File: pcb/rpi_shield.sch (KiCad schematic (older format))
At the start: 7 parts, among them P101 CONN_01X08, P102 CONN_02X20

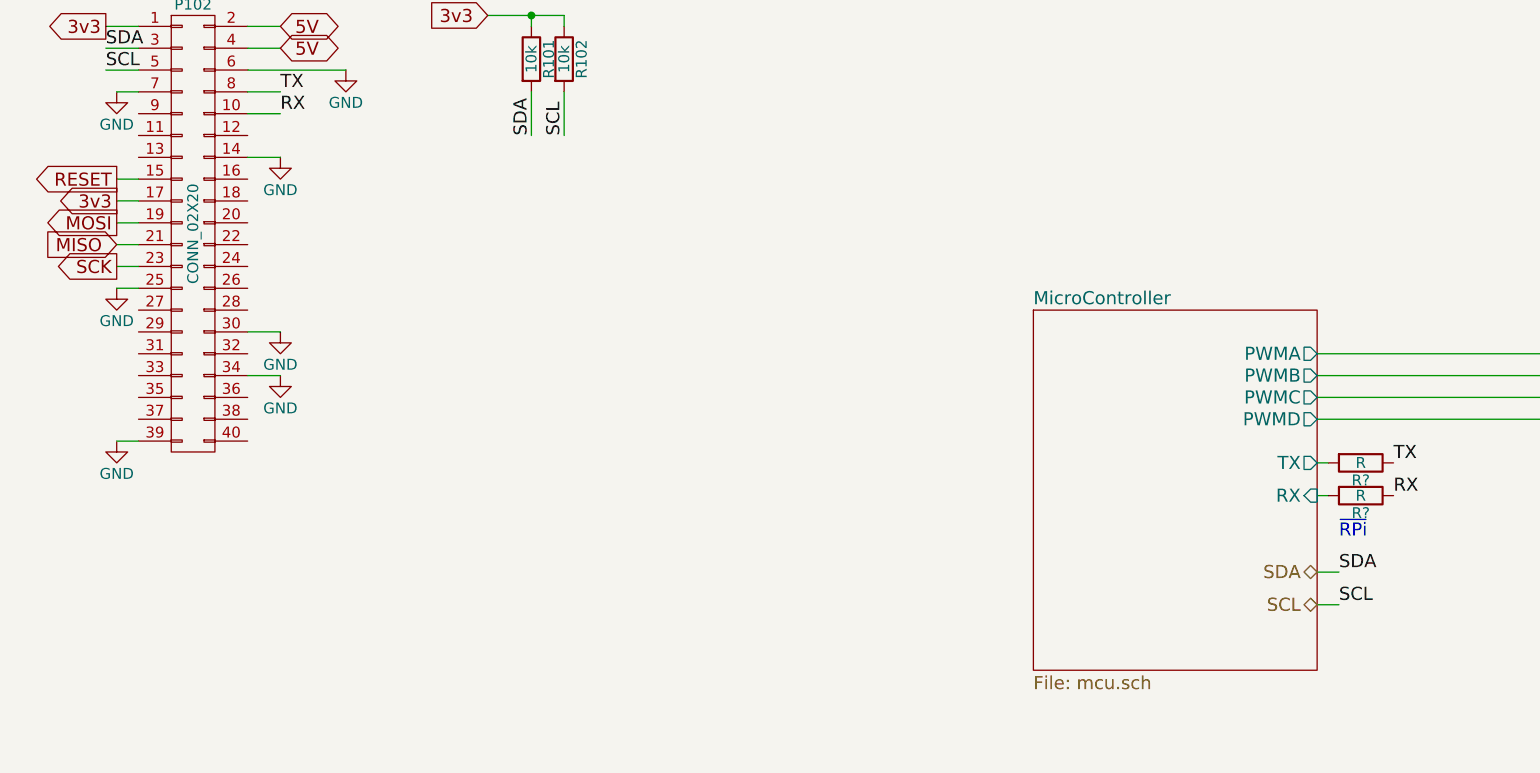
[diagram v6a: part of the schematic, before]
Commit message: removed resistor dividors, added cap to usb
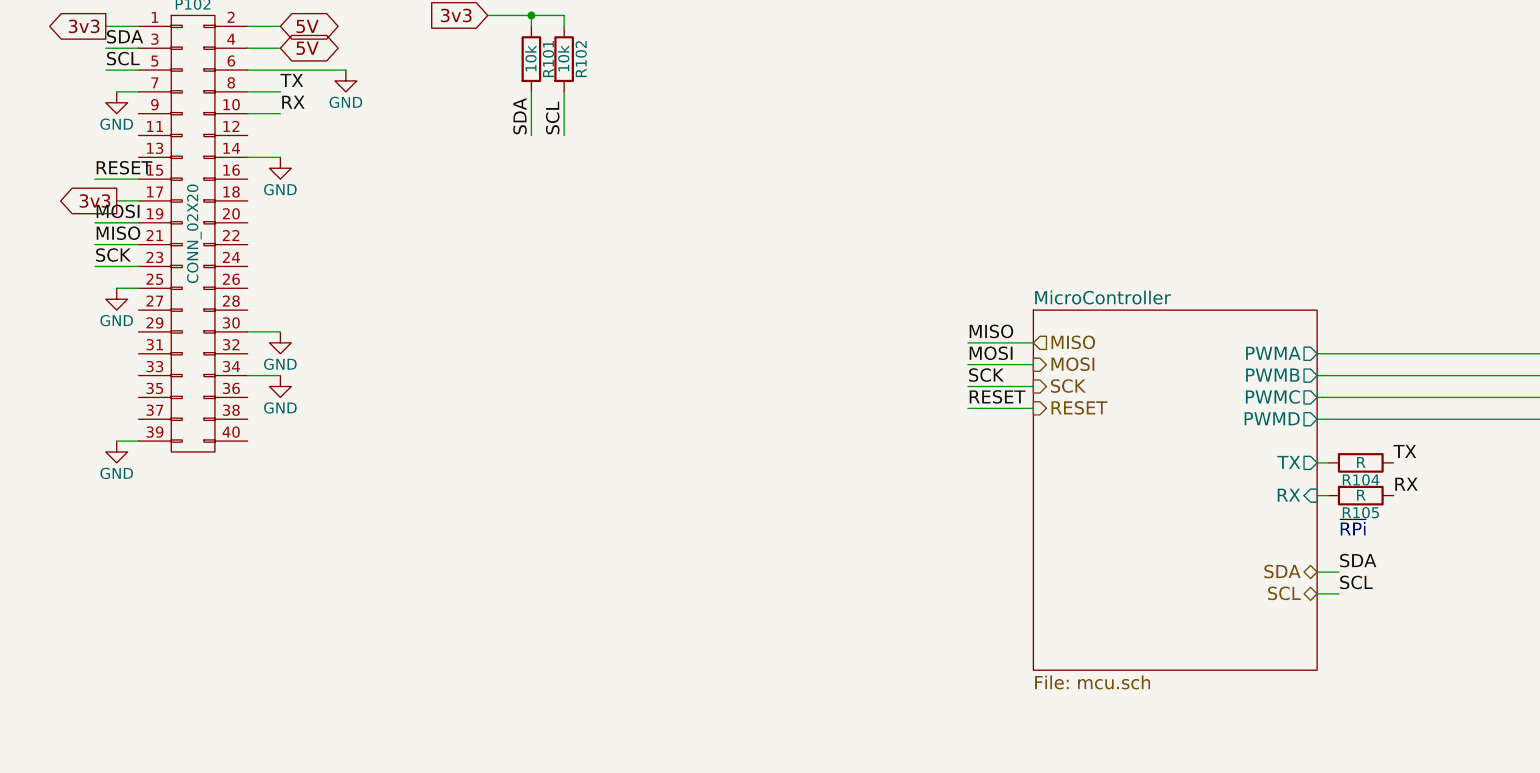
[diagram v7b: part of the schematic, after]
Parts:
- R104, R105: renamed from R?; footprint (none) -> netl:SMD_0603
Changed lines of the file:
@@
 	1500 1200 1350 1200
 $Comp
-L GND #PWR107
+L GND #PWR01
 U 1 1 566A0FDB
 P 2450 1400
-F 0 "#PWR107" H 2450 1150 50  0001 C CNN
+F 0 "#PWR01" H 2450 1150 50  0001 C CNN
 F 1 "GND" H 2450 1250 50  0000 C CNN
 F 2 "" H 2450 1400 60  0000 C CNN
@@
 $EndComp
 $Comp
-L GND #PWR101
+L GND #PWR02
 U 1 1 566A102A
 P 1400 1500
-F 0 "#PWR101" H 1400 1250 50  0001 C CNN
+F 0 "#PWR02" H 1400 1250 50  0001 C CNN
 F 1 "GND" H 1400 1350 50  0000 C CNN
 F 2 "" H 1400 1500 60  0000 C CNN
@@
 	2450 1400 2000 1400
 $Comp
-L GND #PWR104
+L GND #PWR03
 U 1 1 566A10C5
 P 2150 1800
-F 0 "#PWR104" H 2150 1550 50  0001 C CNN
+F 0 "#PWR03" H 2150 1550 50  0001 C CNN
 F 1 "GND" H 2150 1650 50  0000 C CNN
 F 2 "" H 2150 1800 60  0000 C CNN
@@
 	2150 1800 2000 1800
 $Comp
-L GND #PWR105
+L GND #PWR04
 U 1 1 566A110F
 P 2150 2600
-F 0 "#PWR105" H 2150 2350 50  0001 C CNN
+F 0 "#PWR04" H 2150 2350 50  0001 C CNN
 F 1 "GND" H 2150 2450 50  0000 C CNN
 F 2 "" H 2150 2600 60  0000 C CNN
@@
 	2150 2600 2000 2600
 $Comp
-L GND #PWR106
+L GND #PWR05
 U 1 1 566A116A
 P 2150 2800
-F 0 "#PWR106" H 2150 2550 50  0001 C CNN
+F 0 "#PWR05" H 2150 2550 50  0001 C CNN
 F 1 "GND" H 2150 2650 50  0000 C CNN
 F 2 "" H 2150 2800 60  0000 C CNN
@@
 	2150 2800 2000 2800
 $Comp
-L GND #PWR103
+L GND #PWR06
 U 1 1 566A11B6
 P 1400 3100
-F 0 "#PWR103" H 1400 2850 50  0001 C CNN
+F 0 "#PWR06" H 1400 2850 50  0001 C CNN
 F 1 "GND" H 1400 2950 50  0000 C CNN
 F 2 "" H 1400 3100 60  0000 C CNN
@@
 	1500 3100 1400 3100
 $Comp
-L GND #PWR102
+L GND #PWR07
 U 1 1 566A1203
 P 1400 2400
-F 0 "#PWR102" H 1400 2150 50  0001 C CNN
+F 0 "#PWR07" H 1400 2150 50  0001 C CNN
 F 1 "GND" H 1400 2250 50  0000 C CNN
 F 2 "" H 1400 2400 60  0000 C CNN
@@
 Wire Wire Line
 	1500 2000 1400 2000
-Text GLabel 1400 2300 0    60   Output ~ 0
-SCK
-Text GLabel 1400 2100 0    60   Output ~ 0
-MOSI
-Text GLabel 1400 2200 0    60   Input ~ 0
-MISO
-Wire Wire Line
-	1500 2300 1400 2300
-Wire Wire Line
-	1400 2200 1500 2200
-Wire Wire Line
-	1500 2100 1400 2100
-Text GLabel 1400 1900 0    60   Output ~ 0
-RESET
-Wire Wire Line
-	1500 1900 1400 1900
+Wire Wire Line
+	1500 2300 1300 2300
+Wire Wire Line
+	1300 2200 1500 2200
+Wire Wire Line
+	1500 2100 1300 2100
+Wire Wire Line
+	1500 1900 1300 1900
 $Sheet
 S 9150 1350 1100 1850
@@
 $EndComp
 $Comp
-L GND #PWR108
+L GND #PWR08
 U 1 1 56C24834
 P 8050 1250
-F 0 "#PWR108" H 8050 1000 50  0001 C CNN
+F 0 "#PWR08" H 8050 1000 50  0001 C CNN
 F 1 "GND" H 8050 1100 50  0000 C CNN
 F 2 "" H 8050 1250 60  0000 C CNN
@@
 	9150 3000 6900 3000
 $Comp
-L R R?
+L R R104
 U 1 1 570D5FBE
 P 7100 3200
-F 0 "R?" V 7180 3200 50  0000 C CNN
+F 0 "R104" V 7180 3200 50  0000 C CNN
 F 1 "R" V 7100 3200 50  0000 C CNN
-F 2 "" V 7030 3200 50  0000 C CNN
+F 2 "netl:SMD_0603" V 7030 3200 50  0001 C CNN
 F 3 "" H 7100 3200 50  0000 C CNN
 	1    7100 3200
@@
 $EndComp
 $Comp
-L R R?
+L R R105
 U 1 1 570D60AE
 P 7100 3350
-F 0 "R?" V 7180 3350 50  0000 C CNN
+F 0 "R105" V 7180 3350 50  0000 C CNN
 F 1 "R" V 7100 3350 50  0000 C CNN
-F 2 "" V 7030 3350 50  0000 C CNN
+F 2 "netl:SMD_0603" V 7030 3350 50  0001 C CNN
 F 3 "" H 7100 3350 50  0000 C CNN
 	1    7100 3350
@@
 Text HLabel 6900 3700 0    60   BiDi ~ 0
 SDA
-Text HLabel 6900 3850 0    60   BiDi ~ 0
+Text HLabel 6900 3800 0    60   BiDi ~ 0
 SCL
 Text Label 7000 3700 0    60   ~ 0
@@
 	6900 3700 7000 3700
 Wire Wire Line
-	6900 3850 7000 3850
-Text Label 7000 3850 0    60   ~ 0
+	6900 3800 7000 3800
+Text Label 7000 3800 0    60   ~ 0
 SCL
 Text Label 3300 1700 1    60   ~ 0
@@
 Wire Wire Line
 	9150 2450 8950 2450
+Text HLabel 5600 2650 2    60   Input ~ 0
+MISO
+Text HLabel 5600 2750 2    60   Output ~ 0
+MOSI
+Text HLabel 5600 2850 2    60   Output ~ 0
+SCK
+Text HLabel 5600 2950 2    60   Output ~ 0
+RESET
+Text Label 1300 2100 0    60   ~ 0
+MOSI
+Text Label 1300 2200 0    60   ~ 0
+MISO
+Text Label 1300 2300 0    60   ~ 0
+SCK
+Text Label 1300 1900 0    60   ~ 0
+RESET
+Wire Wire Line
+	5600 2650 5300 2650
+Wire Wire Line
+	5600 2750 5300 2750
+Wire Wire Line
+	5600 2850 5300 2850
+Wire Wire Line
+	5600 2950 5300 2950
+Text Label 5300 2950 0    60   ~ 0
+RESET
+Text Label 5300 2750 0    60   ~ 0
+MOSI
+Text Label 5300 2650 0    60   ~ 0
+MISO
+Text Label 5300 2850 0    60   ~ 0
+SCK
 $EndSCHEMATC

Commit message: added mcu
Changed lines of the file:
@@
 VCC
 Wire Wire Line
-	8250 1150 8250 1250
-Wire Wire Line
-	8250 1250 8250 1300
+	8250 1150 8250 1300
 Wire Wire Line
 	8150 1150 8150 1250
@@
 3v3
 Wire Wire Line
-	3100 1150 3300 1150
-Wire Wire Line
-	3300 1150 3450 1150
+	3100 1150 3450 1150
 Wire Wire Line
 	3450 1150 3450 1200
@@
 	3300 1200 3300 1150
 Connection ~ 3300 1150
-$Sheet
-S 5600 2500 1300 1650
-U 570D51C9
-F0 "MicroController" 60
-F1 "mcu.sch" 60
-F2 "PWMA" O R 6900 2700 60
-F3 "PWMB" O R 6900 2800 60
-F4 "PWMC" O R 6900 2900 60
-F5 "PWMD" O R 6900 3000 60
-F6 "TX" O R 6900 3200 60
-F7 "RX" I R 6900 3350 60
-$EndSheet
 Wire Wire Line
 	6900 2700 9150 2700
@@
 Text Notes 7000 3550 0    60   ~ 0
 ~RPi
-Text HLabel 6900 3700 0    60   BiDi ~ 0
-SDA
-Text HLabel 6900 3800 0    60   BiDi ~ 0
-SCL
 Text Label 7000 3700 0    60   ~ 0
 SDA
@@
 Wire Wire Line
 	9150 2450 8950 2450
-Text HLabel 5600 2650 2    60   Input ~ 0
-MISO
-Text HLabel 5600 2750 2    60   Output ~ 0
-MOSI
-Text HLabel 5600 2850 2    60   Output ~ 0
-SCK
-Text HLabel 5600 2950 2    60   Output ~ 0
-RESET
 Text Label 1300 2100 0    60   ~ 0
 MOSI
@@
 Text Label 5300 2850 0    60   ~ 0
 SCK
+$Sheet
+S 5600 2500 1300 1650
+U 570D51C9
+F0 "MicroController" 60
+F1 "mcu.sch" 60
+F2 "PWMA" O R 6900 2700 60
+F3 "PWMB" O R 6900 2800 60
+F4 "PWMC" O R 6900 2900 60
+F5 "PWMD" O R 6900 3000 60
+F6 "TX" O R 6900 3200 60
+F7 "RX" I R 6900 3350 60
+F8 "~RESET" I L 5600 2950 60
+F9 "MISO" O L 5600 2650 60
+F10 "MOSI" I L 5600 2750 60
+F11 "SCK" I L 5600 2850 60
+F12 "SDA" O R 6900 3700 60
+F13 "SCL" O R 6900 3800 60
+$EndSheet
 $EndSCHEMATC
